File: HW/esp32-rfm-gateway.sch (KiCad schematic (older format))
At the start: 61 parts, among them J1 Res, J2 Boot, J20 220V~, J21 c5V, J22 s14500, J23 s18650, J24 cPS, J25 c3V3, J3 PinDbg, J30 AntSMA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

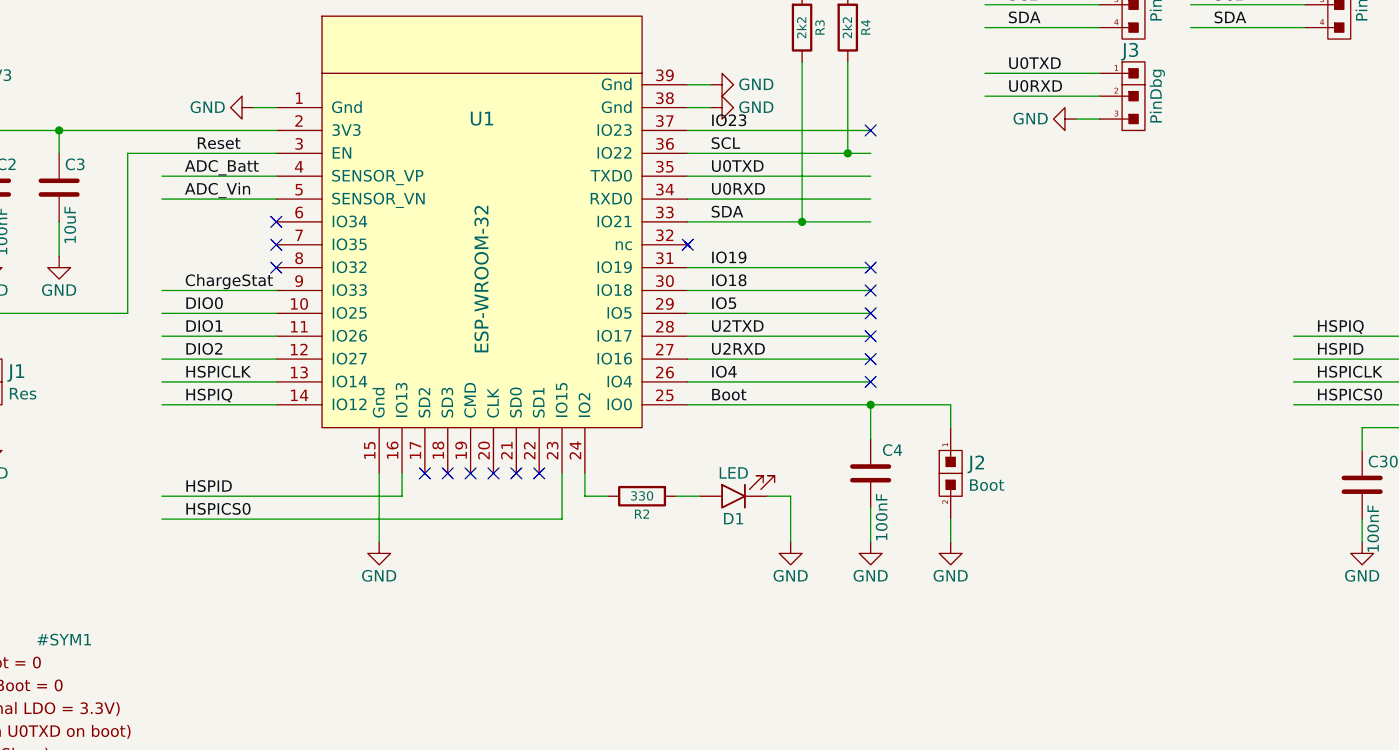
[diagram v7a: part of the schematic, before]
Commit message: Changes the schematic to add a header for USART2 and two buttons
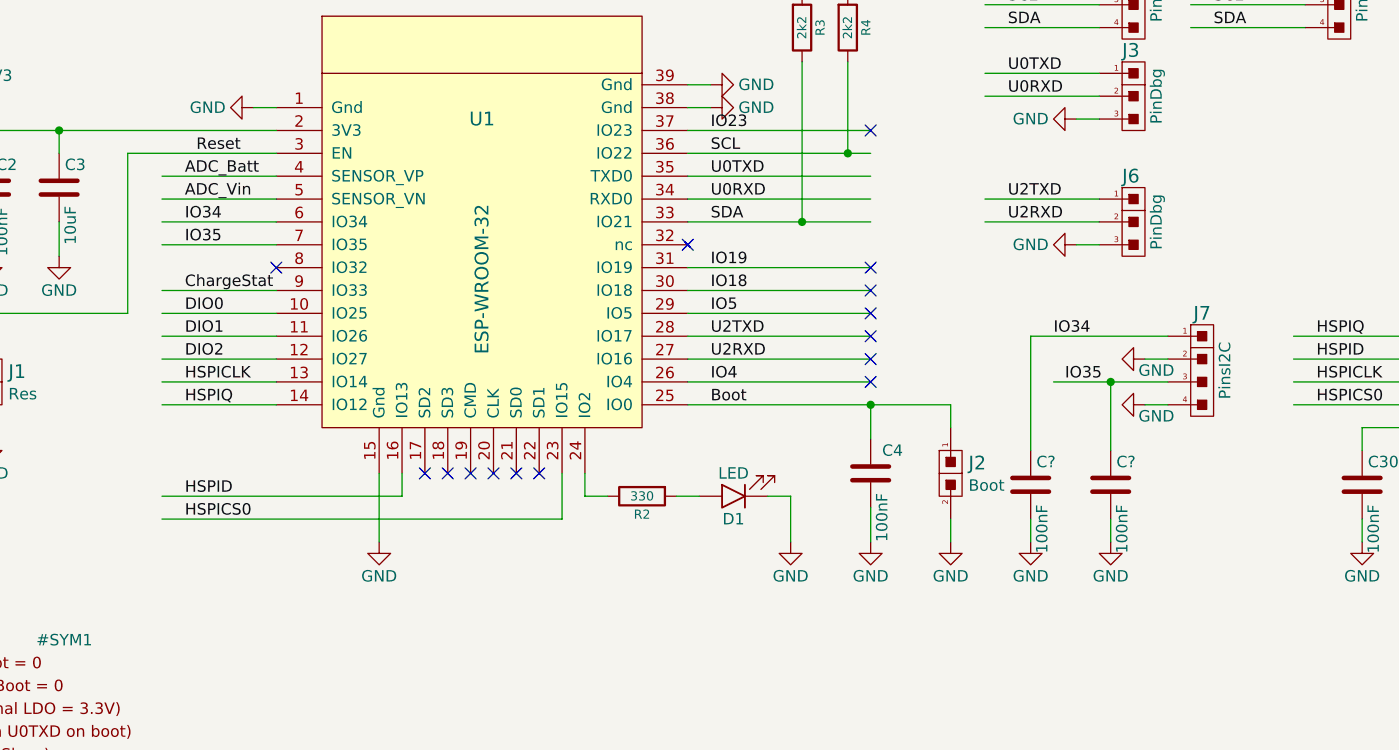
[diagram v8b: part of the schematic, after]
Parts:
- added C? (x2): 100nF, CalinGeneric:C0805HS, symbol Device:C
- added J6: PinDbg, CalinConnectors:Pin_Header_Straight_1x03_Cyan, symbol calin:CS_3
- added J7: PinsI2C, CalinConnectors:Pin_Header_Straight_1x04, symbol calin:CS_4
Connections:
- net labels added: IO34, IO35
- wire segments 222 -> 236
- no-connect marks 20 -> 18
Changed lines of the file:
@@
 Text Label 5450 2800 0    50   ~ 0
 IO4
-NoConn ~ 3550 2100
-NoConn ~ 3550 2200
 $Comp
 L calin:TLV379IDBV U24
@@
 Text Label 9650 1800 0    50   ~ 0
 SDA
+$Comp
+L calin:CS_4 J7
+U 1 1 5CB934F2
+P 7600 2750
+F 0 "J7" H 7600 3000 60  0000 C CNN
+F 1 "PinsI2C" V 7700 2750 50  0000 C CNN
+F 2 "CalinConnectors:Pin_Header_Straight_1x04" H 7600 2900 60  0001 C CNN
+F 3 "" H 7600 2900 60  0000 C CNN
+	1    7600 2750
+	1    0    0    -1
+$EndComp
+$Comp
+L calin:CS_3 J6
+U 1 1 5CB93990
+P 7300 2100
+F 0 "J6" H 7250 2300 60  0000 L CNN
+F 1 "PinDbg" V 7400 2100 50  0000 C CNN
+F 2 "CalinConnectors:Pin_Header_Straight_1x03_Cyan" H 7300 2200 60  0001 C CNN
+F 3 "" H 7300 2200 60  0000 C CNN
+	1    7300 2100
+	1    0    0    -1
+$EndComp
+Wire Wire Line
+	7150 2000 6650 2000
+Wire Wire Line
+	7150 2100 6650 2100
+$Comp
+L power:GND #PWR?
+U 1 1 5CBC7809
+P 7350 2700
+F 0 "#PWR?" H 7350 2450 50  0001 C CNN
+F 1 "GND" V 7400 2750 50  0000 C CNN
+F 2 "" H 7350 2700 50  0000 C CNN
+F 3 "" H 7350 2700 50  0000 C CNN
+	1    7350 2700
+	0    1    1    0
+$EndComp
+$Comp
+L power:GND #PWR?
+U 1 1 5CBC78CB
+P 7350 2900
+F 0 "#PWR?" H 7350 2650 50  0001 C CNN
+F 1 "GND" V 7400 2950 50  0000 C CNN
+F 2 "" H 7350 2900 50  0000 C CNN
+F 3 "" H 7350 2900 50  0000 C CNN
+	1    7350 2900
+	0    1    1    0
+$EndComp
+$Comp
+L power:GND #PWR?
+U 1 1 5CBC798D
+P 7050 2200
+F 0 "#PWR?" H 7050 1950 50  0001 C CNN
+F 1 "GND" V 7050 2000 50  0000 C CNN
+F 2 "" H 7050 2200 50  0000 C CNN
+F 3 "" H 7050 2200 50  0000 C CNN
+	1    7050 2200
+	0    1    1    0
+$EndComp
+Wire Wire Line
+	7350 2700 7450 2700
+Wire Wire Line
+	7350 2900 7450 2900
+Wire Wire Line
+	7050 2200 7150 2200
+Text Label 6750 2000 0    50   ~ 0
+U2TXD
+Text Label 6750 2100 0    50   ~ 0
+U2RXD
+Wire Wire Line
+	3550 2100 3050 2100
+Wire Wire Line
+	3550 2200 3050 2200
+Text Label 3150 2100 0    50   ~ 0
+IO34
+Text Label 3150 2200 0    50   ~ 0
+IO35
+Text Label 6950 2600 0    50   ~ 0
+IO34
+Text Label 7000 2800 0    50   ~ 0
+IO35
+$Comp
+L Device:C C?
+U 1 1 5CC0C4F0
+P 6850 3250
+F 0 "C?" H 6875 3350 50  0000 L CNN
+F 1 "100nF" V 6900 2950 50  0000 L CNN
+F 2 "CalinGeneric:C0805HS" H 6888 3100 50  0001 C CNN
+F 3 "" H 6850 3250 50  0000 C CNN
+	1    6850 3250
+	1    0    0    -1
+$EndComp
+$Comp
+L power:GND #PWR?
+U 1 1 5CC0C4F6
+P 6850 3500
+F 0 "#PWR?" H 6850 3250 50  0001 C CNN
+F 1 "GND" H 6850 3350 50  0000 C CNN
+F 2 "" H 6850 3500 50  0000 C CNN
+F 3 "" H 6850 3500 50  0000 C CNN
+	1    6850 3500
+	1    0    0    -1
+$EndComp
+Wire Wire Line
+	6850 3400 6850 3500
+$Comp
+L Device:C C?
+U 1 1 5CC289FE
+P 7200 3250
+F 0 "C?" H 7225 3350 50  0000 L CNN
+F 1 "100nF" V 7250 2950 50  0000 L CNN
+F 2 "CalinGeneric:C0805HS" H 7238 3100 50  0001 C CNN
+F 3 "" H 7200 3250 50  0000 C CNN
+	1    7200 3250
+	1    0    0    -1
+$EndComp
+$Comp
+L power:GND #PWR?
+U 1 1 5CC28A04
+P 7200 3500
+F 0 "#PWR?" H 7200 3250 50  0001 C CNN
+F 1 "GND" H 7200 3350 50  0000 C CNN
+F 2 "" H 7200 3500 50  0000 C CNN
+F 3 "" H 7200 3500 50  0000 C CNN
+	1    7200 3500
+	1    0    0    -1
+$EndComp
+Wire Wire Line
+	7200 3400 7200 3500
+Wire Wire Line
+	7450 2600 6850 2600
+Wire Wire Line
+	6850 2600 6850 3100
+Wire Wire Line
+	7450 2800 7200 2800
+Wire Wire Line
+	7200 2800 7200 3100
+Wire Wire Line
+	7200 2800 6950 2800
+Connection ~ 7200 2800
 $EndSCHEMATC
